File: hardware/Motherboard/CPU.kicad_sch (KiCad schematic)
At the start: 20 parts, among them U1 MC6809, U10 74LS138, U2 27C64, U3 74LS245, U4 74LS139, U5 74LS20, U6 74LS08, U66 74LS273, U7 74LS02, U8 74LS00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

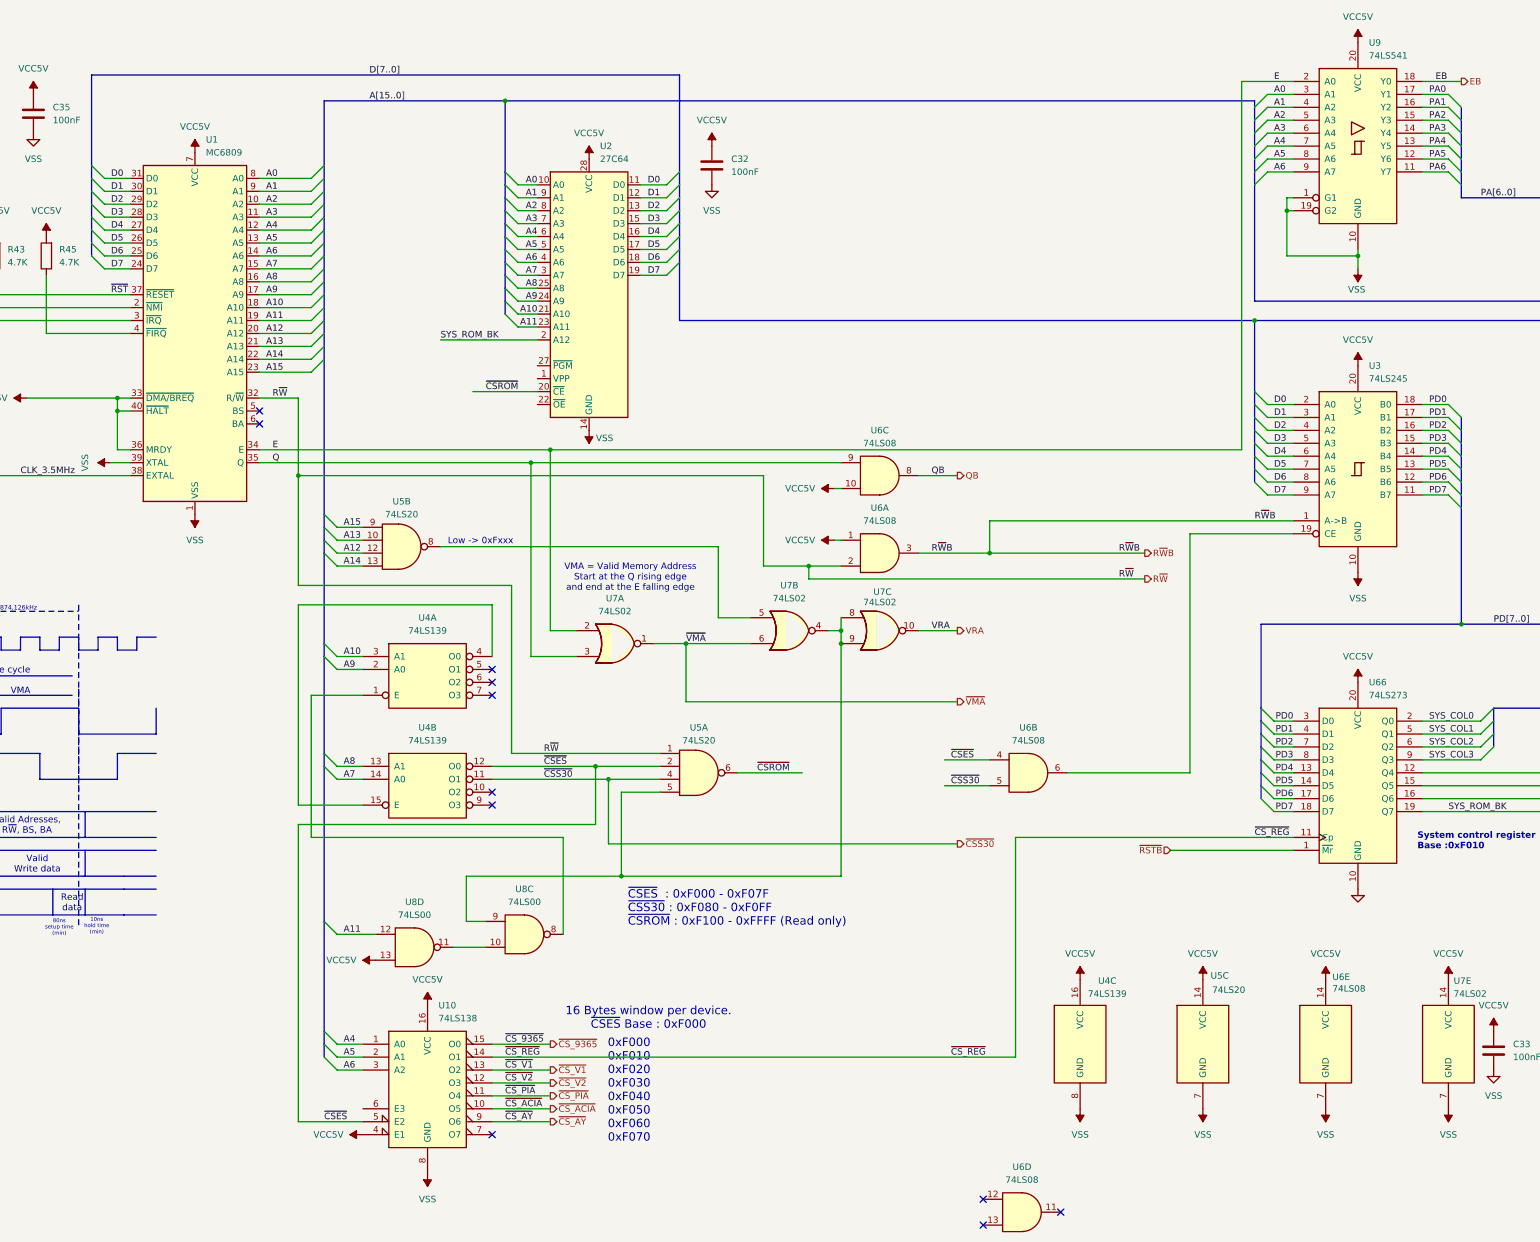
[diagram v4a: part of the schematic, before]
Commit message: Fix buffer direction
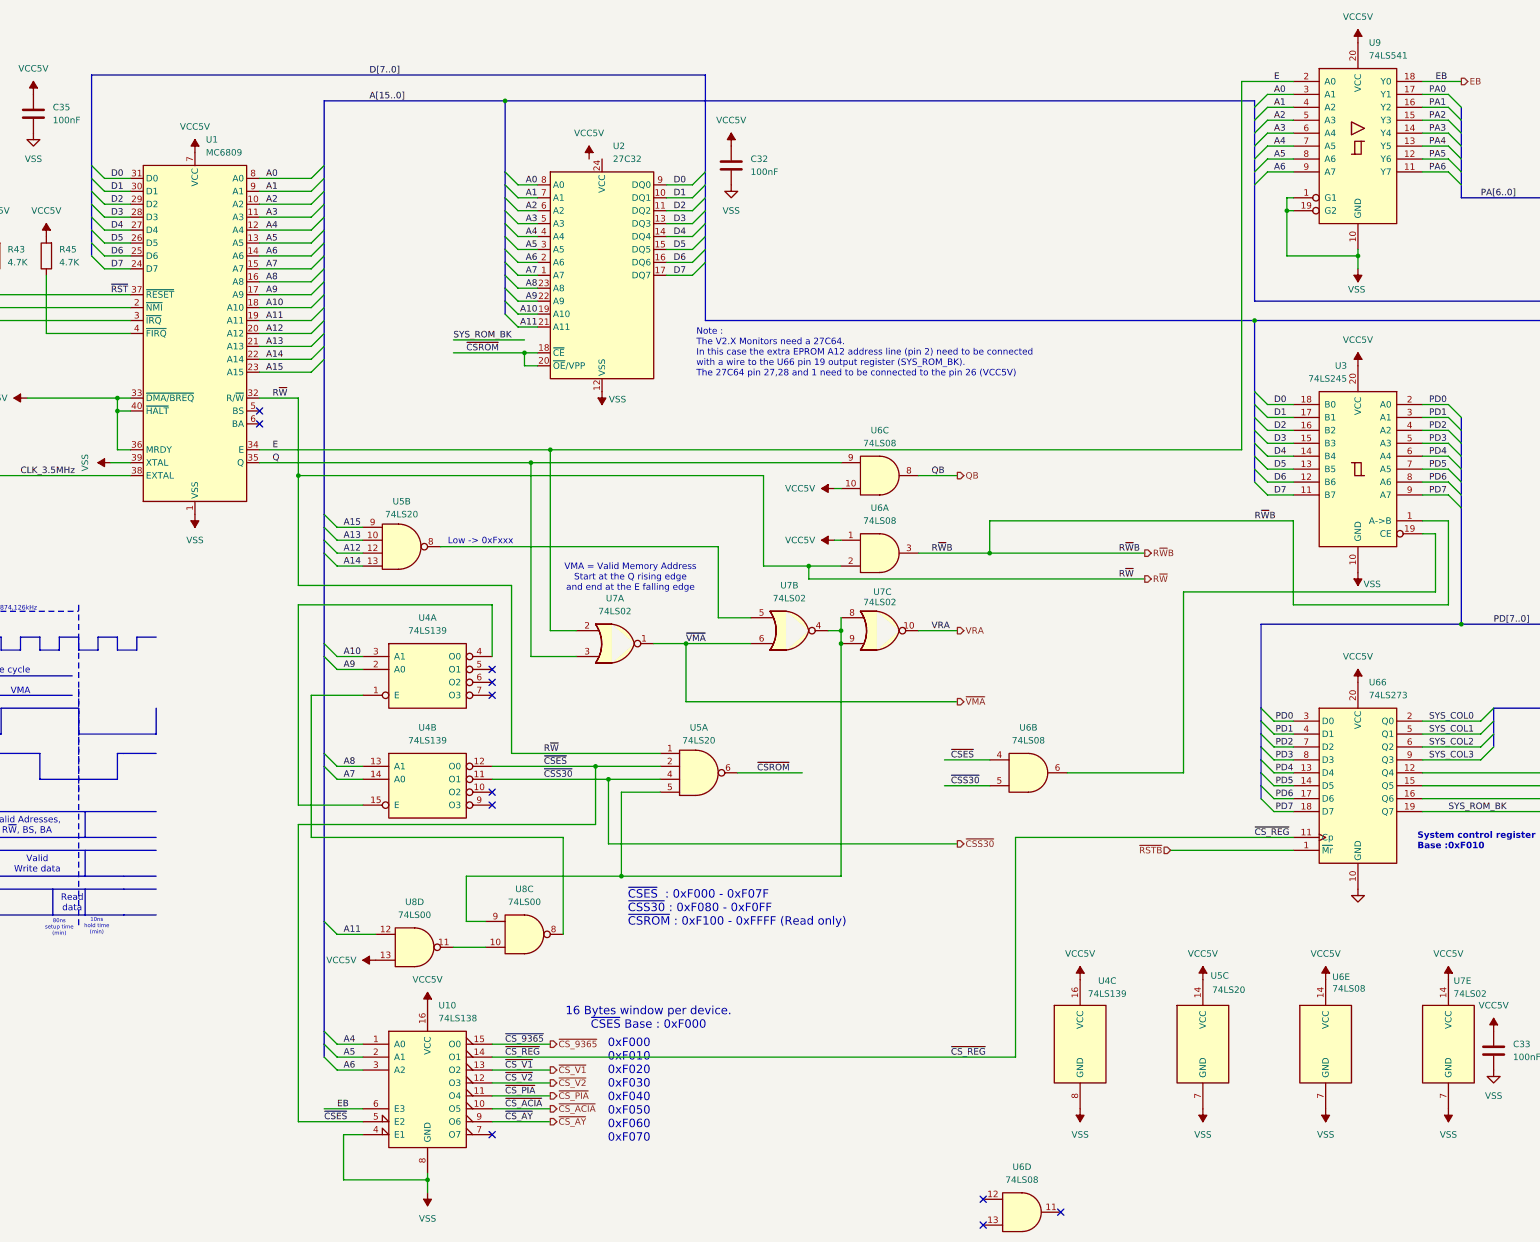
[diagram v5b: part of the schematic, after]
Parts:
- removed U2: 27C64, Package_DIP:DIP-28_W15.24mm_Socket, symbol Memory_EPROM:27C64
- added U2: 27C32, Package_DIP:DIP-24_18.0mmx34.29mm_W15.24mm, symbol Memory_RAM:M48Tx2
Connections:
- net A0: now also U2.8 (A0)
- net A1: now also U2.7 (A1)
- net A10: now also U2.19 (A10)
- net A11: now also U2.21 (A11)
- net A2: now also U2.6 (A2)
- net A3: now also U2.5 (A3)
- net A4: now also U2.4 (A4)
- net A5: now also U2.3 (A5)
- net A6: now also U2.2 (A6)
- net A7: now also U2.1 (A7)
- net A8: now also U2.23 (A8)
- net A9: now also U2.22 (A9)
- net D0: now also U3.18 (B0), U2.9 (DQ0); no longer U3.2 (A0)
- net D1: now also U3.17 (B1), U2.10 (DQ1); no longer U3.3 (A1)
- net D2: now also U3.16 (B2), U2.11 (DQ2); no longer U3.4 (A2)
- net D3: now also U3.15 (B3), U2.13 (DQ3); no longer U3.5 (A3)
- net D4: now also U3.14 (B4), U2.14 (DQ4); no longer U3.6 (A4)
- net D5: now also U3.13 (B5), U2.15 (DQ5); no longer U3.7 (A5)
- net D6: now also U3.12 (B6), U2.16 (DQ6); no longer U3.8 (A6)
- net D7: now also U3.11 (B7), U2.17 (DQ7); no longer U3.9 (A7)
- net EB: now also U10.6 (E3)
- net PD0: now also U3.2 (A0); no longer U3.18 (B0)
- net PD1: now also U3.3 (A1); no longer U3.17 (B1)
- net PD2: now also U3.4 (A2); no longer U3.16 (B2)
- net PD3: now also U3.5 (A3); no longer U3.15 (B3)
- net PD4: now also U3.6 (A4); no longer U3.14 (B4)
- net PD5: now also U3.7 (A5); no longer U3.13 (B5)
- net PD6: now also U3.8 (A6); no longer U3.12 (B6)
- net PD7: now also U3.9 (A7); no longer U3.11 (B7)
- net VCC5V: no longer U10.4 (E1)
- net VSS: now also U10.4 (E1), U2.12 (VSS)
- net ~{CSROM}: now also U2.18 (~{CE}), U2.20 (~{OE}/VPP)
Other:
- note added: "Note : The V2.X Monitors need a 27C64. In this case the extra EPROM A12 address line (pin 2) need to be connected with a wire to the U66 pin 19 output register (SYS_ROM_BK). The 27C64 pin 27,28 and 1 need to be connected to the pin 26 (VCC5V)"
- moved on the sheet: C32

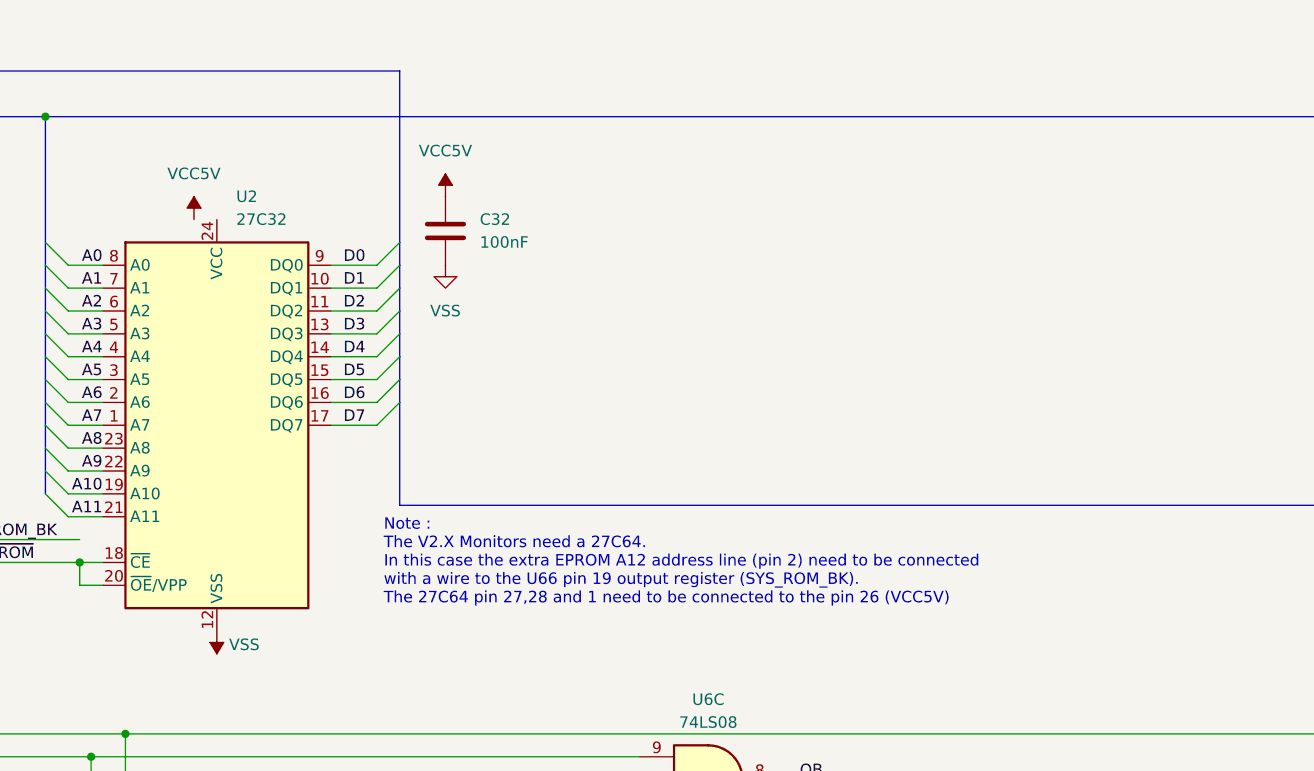
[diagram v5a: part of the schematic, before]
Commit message: eprom vcc fix.
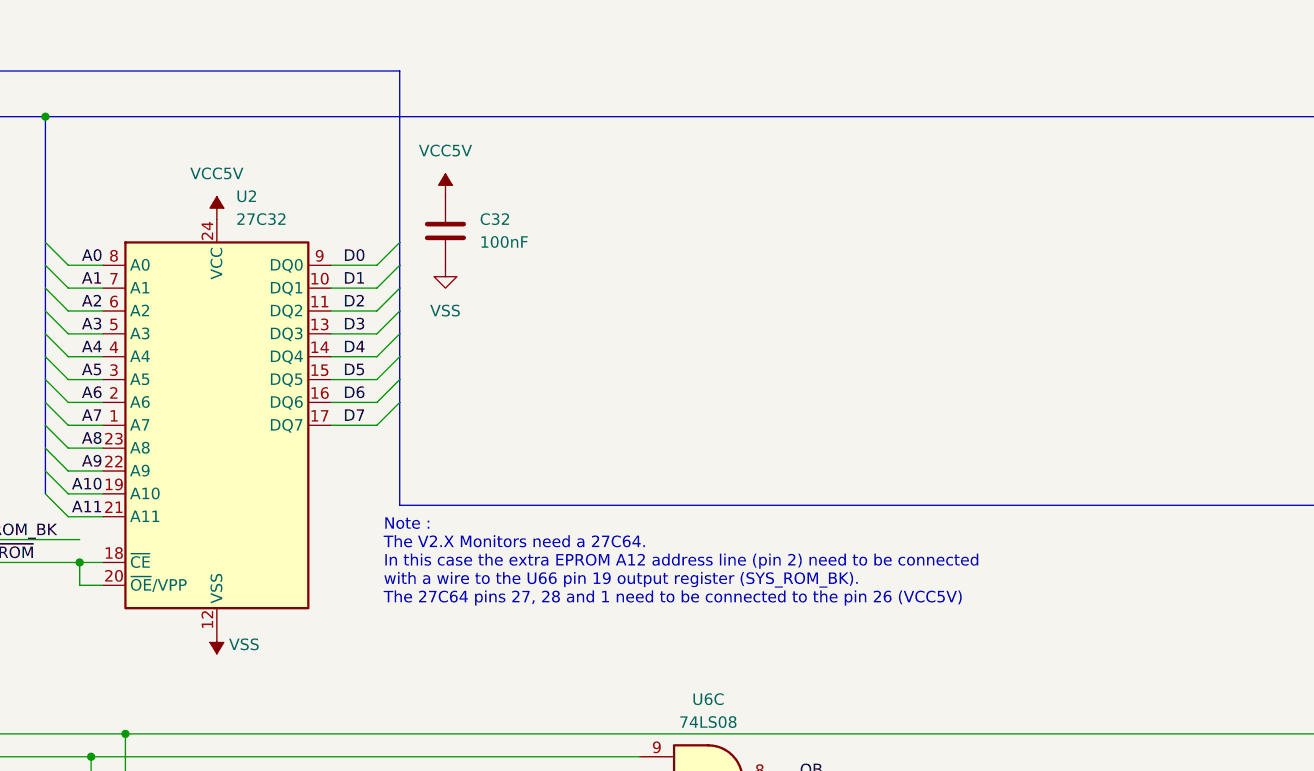
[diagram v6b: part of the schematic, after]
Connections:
- net VCC5V: now also U2.24 (VCC)
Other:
- note added: "Note : The V2.X Monitors need a 27C64. In this case the extra EPROM A12 address line (pin 2) need to be connected with a wire to the U66 pin 19 output register (SYS_ROM_BK). The 27C64 pins 27, 28 and 1 need to be connected to the pin 26 (VCC5V)"
- note removed: "Note : The V2.X Monitors need a 27C64. In this case the extra EPROM A12 address line (pin 2) need to be connected with a wire to the U66 pin 19 output register (SYS_ROM_BK). The 27C64 pin 27,28 and 1 need to be connected to the pin 26 (VCC5V)"
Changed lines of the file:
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@@
 		(comment 3 "Drawn by Jean-François DEL NERO")
 	)
-	(text "Note :\nThe V2.X Monitors need a 27C64.\nIn this case the extra EPROM A12 address line (pin 2) need to be connected \nwith a wire to the U66 pin 19 output register (SYS_ROM_BK).\nThe 27C64 pin 27,28 and 1 need to be connected to the pin 26 (VCC5V)"
+	(text "Note :\nThe V2.X Monitors need a 27C64.\nIn this case the extra EPROM A12 address line (pin 2) need to be connected \nwith a wire to the U66 pin 19 output register (SYS_ROM_BK).\nThe 27C64 pins 27, 28 and 1 need to be connected to the pin 26 (VCC5V)"
 		(exclude_from_sim no)
 		(at 220.472 91.44 0)
@@
 	(symbol
 		(lib_id "power:VSS")
-		(at 199.39 53.34 0)
+		(at 201.93 53.34 0)
 		(unit 1)
 		(exclude_from_sim no)
@@
 		(fields_autoplaced yes)
 		(property "Reference" "#PWR0129"
-			(at 199.39 57.15 0)
+			(at 201.93 57.15 0)
 			(effects
 				(font
@@
 		)
 		(property "Value" "VCC5V"
-			(at 199.39 48.26 0)
+			(at 201.93 48.26 0)
 			(effects
 				(font
@@
 		)
 		(property "Footprint" ""
-			(at 199.39 53.34 0)
+			(at 201.93 53.34 0)
 			(effects
 				(font
@@
 		)
 		(property "Datasheet" ""
-			(at 199.39 53.34 0)
+			(at 201.93 53.34 0)
 			(effects
 				(font
@@
 		)
 		(property "Description" "Power symbol creates a global label with name \"VSS\""
-			(at 199.39 53.34 0)
+			(at 201.93 53.34 0)
 			(effects
 				(font

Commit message: Connectors footprint.
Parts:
- D3: footprint Diode_THT:D_DO-35_SOD27_P7.62mm_Horizontal -> Diode_THT:D_DO-35_SOD27_P12.70mm_Horizontal
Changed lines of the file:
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@@
 			)
 		)
-		(property "Footprint" "Diode_THT:D_DO-35_SOD27_P7.62mm_Horizontal"
+		(property "Footprint" "Diode_THT:D_DO-35_SOD27_P12.70mm_Horizontal"
 			(at 45.72 60.96 0)
 			(effects

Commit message: more fixes !
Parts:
- U2: footprint Package_DIP:DIP-24_18.0mmx34.29mm_W15.24mm -> Package_DIP:DIP-24_W15.24mm_Socket
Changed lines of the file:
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@@
 			)
 		)
-		(property "Footprint" "Package_DIP:DIP-24_18.0mmx34.29mm_W15.24mm"
+		(property "Footprint" "Package_DIP:DIP-24_W15.24mm_Socket"
 			(at 200.66 75.946 0)
 			(effects
